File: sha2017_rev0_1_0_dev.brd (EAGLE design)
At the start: 95 x 86 mm, 200 parts, among them IC1 CP210X_USB_UART, IC2 AP7215, IC3 ESP32WROOM32, IC4 MCP73833, IC5 FXL6408, IC6 CPT112, Q2 MMBT2222A, Q3 MMBT2222A, Q4 MMBT2222A, Q5 MMBT2222A, Q6 SI1304 BDL, Q7 MMBT2222A, T1 SI2301DS, T2 SI2301DS, T3 SI2301DS, X1 2908-05WB-MG, X3 JST-PH3

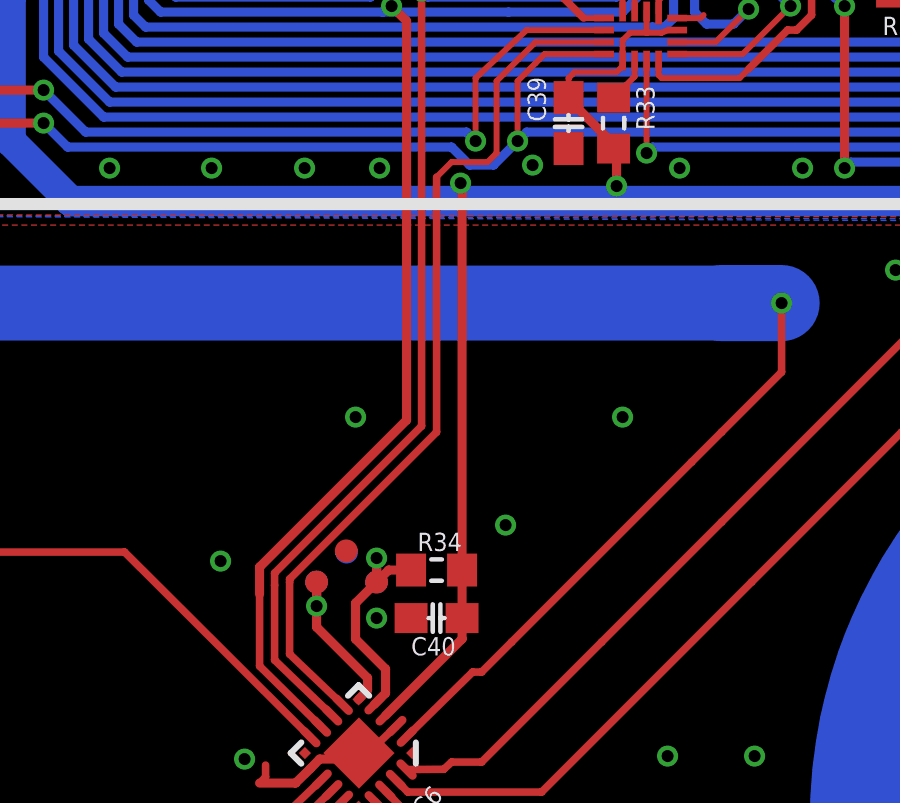
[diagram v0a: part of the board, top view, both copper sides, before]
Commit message: added 4,7µF decopling capacitor to the cpt112s power rails
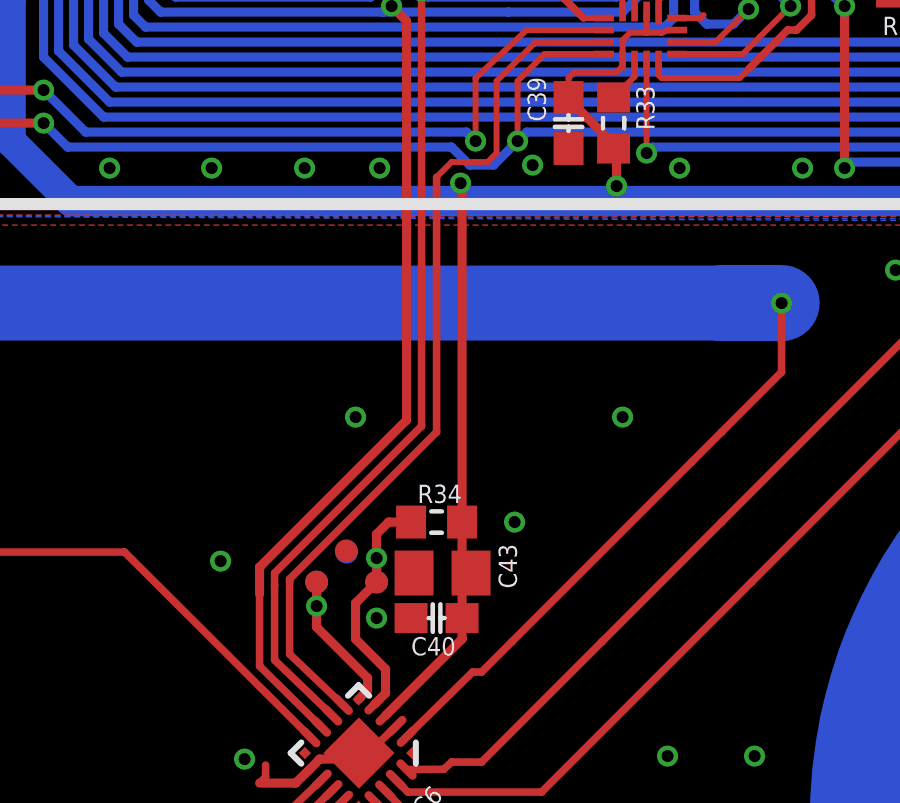
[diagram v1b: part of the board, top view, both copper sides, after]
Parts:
- added C43: 4u7/16V, rcl:C0805
- moved R34 1.60 mm to (43.5, 30.0)
- moved $$U$1 0.32 mm to (46.1, 30.0)
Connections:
- net +3V3: now also C43.1
- net GND: now also C43.2
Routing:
- net N$61: track 7.84 -> 8.64 mm
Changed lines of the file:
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@@
 <attribute name="PARTNO" value="NAP" x="39.5" y="28" size="1.778" layer="27" display="off"/>
 </element>
-<element name="R34" library="sha2017_rev0_1_0_dev" package="R0603-DASHES" value="1k" x="43.5" y="28.4" smashed="yes">
-<attribute name="NAME" x="42.865" y="29.035" size="0.6096" layer="25" font="vector" ratio="16"/>
-<attribute name="VALUE" x="42.865" y="26.495" size="1.27" layer="27"/>
-<attribute name="PARTNO" value="ERJ-3GEYJ102V" x="43.5" y="28.4" size="1.778" layer="27" display="off"/>
+<element name="R34" library="sha2017_rev0_1_0_dev" package="R0603-DASHES" value="1k" x="43.5" y="30" smashed="yes">
+<attribute name="NAME" x="42.865" y="30.635" size="0.6096" layer="25" font="vector" ratio="16"/>
+<attribute name="VALUE" x="42.865" y="28.095" size="1.27" layer="27"/>
+<attribute name="PARTNO" value="ERJ-3GEYJ102V" x="43.5" y="30" size="1.778" layer="27" display="off"/>
 </element>
 <element name="Q7" library="SparkFun-DiscreteSemi" package="SOT23-3" value="MMBT2222A" x="21" y="52.1" smashed="yes" rot="R180">
@@
 <attribute name="PARTNO" value="NAP" x="37.1" y="22.1" size="1.778" layer="27" display="off"/>
 </element>
-<element name="$$U$1" library="badge" package="VIA" value="VIA" x="45.8" y="29.9" smashed="yes">
-<attribute name="PARTNO" value="NAP" x="45.8" y="29.9" size="1.778" layer="27" display="off"/>
+<element name="$$U$1" library="badge" package="VIA" value="VIA" x="46.1" y="30" smashed="yes">
+<attribute name="PARTNO" value="NAP" x="46.1" y="30" size="1.778" layer="27" display="off"/>
 </element>
 <element name="U$4" library="badge" package="VIA" value="VIA" x="28.4" y="33.5" smashed="yes">
@@
 <attribute name="NAME" x="16.892" y="54.67" size="0.8128" layer="25" font="vector" ratio="16"/>
 <attribute name="VALUE" x="16.249" y="57.708" size="0.4064" layer="27" rot="R270"/>
+</element>
+<element name="C43" library="rcl" package="C0805" value="4u7/16V" x="43.7" y="28.3" smashed="yes" rot="R180">
+<attribute name="PARTNO" value="GRM21BR61C475KA88K" x="43.7" y="28.3" size="1.778" layer="27" rot="R180" display="off"/>
+<attribute name="NAME" x="45.57" y="29.27" size="0.6096" layer="25" font="vector" ratio="15" rot="R270"/>
+<attribute name="VALUE" x="44.97" y="30.84" size="1.27" layer="27" rot="R180"/>
 </element>
 </elements>
@@
 <contactref element="TP3" pad="P$1"/>
 <via x="64.9" y="71.32" extent="1-16" drill="0.4"/>
+<contactref element="C43" pad="2"/>
 <wire x1="40.49" y1="29.04" x2="40.5" y2="29" width="0" layer="19" extent="1-16"/>
 </signal>
@@
 <wire x1="49.5" y1="41.2" x2="49.3" y2="41" width="0.3048" layer="16"/>
 <wire x1="49.3" y1="41" x2="49.3" y2="40.7" width="0.3048" layer="16"/>
-<wire x1="44.35" y1="28.4" x2="44.35" y2="26.8" width="0.3048" layer="1"/>
+<wire x1="44.35" y1="30" x2="44.35" y2="28.2" width="0.3048" layer="1"/>
+<wire x1="44.35" y1="28.2" x2="44.35" y2="26.8" width="0.3048" layer="1"/>
 <wire x1="44.35" y1="26.8" x2="44.35" y2="26.10355625" width="0.3048" layer="1"/>
 <wire x1="44.35" y1="26.10355625" x2="41.80455" y2="23.55810625" width="0.3048" layer="1"/>
-<wire x1="44.35" y1="28.4" x2="44.35" y2="41.25" width="0.3048" layer="1"/>
+<wire x1="44.35" y1="30" x2="44.35" y2="41.25" width="0.3048" layer="1"/>
 <wire x1="44.35" y1="41.25" x2="44.3" y2="41.3" width="0.3048" layer="1"/>
 <via x="44.3" y="41.3" extent="1-16" drill="0.4"/>
@@
 <wire x1="20.9" y1="48.6" x2="23.25" y2="48.6" width="0.6096" layer="1"/>
 <wire x1="23.25" y1="48.6" x2="23.8" y2="48.05" width="0.6096" layer="1"/>
+<contactref element="C43" pad="1"/>
+<wire x1="44.65" y1="28.3" x2="44.408578125" y2="28.2" width="0.3048" layer="1" curve="-45"/>
+<wire x1="44.408578125" y1="28.2" x2="44.35" y2="28.2" width="0.3048" layer="1"/>
 </signal>
 <signal name="GDR">
@@
 <wire x1="41.8" y1="24.3" x2="41.8" y2="25.1" width="0.3048" layer="1"/>
 <wire x1="41.8" y1="25.1" x2="40.8" y2="26.1" width="0.3048" layer="1"/>
-<wire x1="41.5" y1="28" x2="41.9" y2="28.4" width="0.3048" layer="1"/>
-<wire x1="41.9" y1="28.4" x2="42.65" y2="28.4" width="0.3048" layer="1"/>
 <contactref element="TP100" pad="P$1"/>
 <wire x1="40.8" y1="26.1" x2="40.8" y2="27.3" width="0.3048" layer="1"/>
@@
 <via x="41.5" y="28.8" extent="1-16" drill="0.4"/>
 <wire x1="41.5" y1="28.8" x2="41.5" y2="28" width="0.3048" layer="16"/>
+<wire x1="42.65" y1="30" x2="41.9" y2="30" width="0.3048" layer="1"/>
+<wire x1="41.9" y1="30" x2="41.5" y2="29.6" width="0.3048" layer="1"/>
+<wire x1="41.5" y1="29.6" x2="41.5" y2="28.8" width="0.3048" layer="1"/>
 </signal>
 <signal name="N$62">

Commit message: minor adjustments
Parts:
- moved C43 0.10 mm to (43.7, 28.4)
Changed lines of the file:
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@@
 <attribute name="VALUE" x="16.249" y="57.708" size="0.4064" layer="27" rot="R270"/>
 </element>
-<element name="C43" library="rcl" package="C0805" value="4u7/16V" x="43.7" y="28.3" smashed="yes" rot="R180">
-<attribute name="PARTNO" value="GRM21BR61C475KA88K" x="43.7" y="28.3" size="1.778" layer="27" rot="R180" display="off"/>
-<attribute name="NAME" x="45.57" y="29.27" size="0.6096" layer="25" font="vector" ratio="15" rot="R270"/>
-<attribute name="VALUE" x="44.97" y="30.84" size="1.27" layer="27" rot="R180"/>
+<element name="C43" library="rcl" package="C0805" value="4u7/16V" x="43.7" y="28.4" smashed="yes" rot="R180">
+<attribute name="PARTNO" value="GRM21BR61C475KA88K" x="43.7" y="28.4" size="1.778" layer="27" rot="R180" display="off"/>
+<attribute name="NAME" x="45.57" y="29.37" size="0.6096" layer="25" font="vector" ratio="15" rot="R270"/>
+<attribute name="VALUE" x="44.97" y="30.94" size="1.27" layer="27" rot="R180"/>
 </element>
 </elements>
@@
 <wire x1="23.25" y1="48.6" x2="23.8" y2="48.05" width="0.6096" layer="1"/>
 <contactref element="C43" pad="1"/>
-<wire x1="44.65" y1="28.3" x2="44.408578125" y2="28.2" width="0.3048" layer="1" curve="-45"/>
+<wire x1="44.65" y1="28.4" x2="44.408578125" y2="28.2" width="0.3048" layer="1" curve="-45"/>
 <wire x1="44.408578125" y1="28.2" x2="44.35" y2="28.2" width="0.3048" layer="1"/>
 </signal>

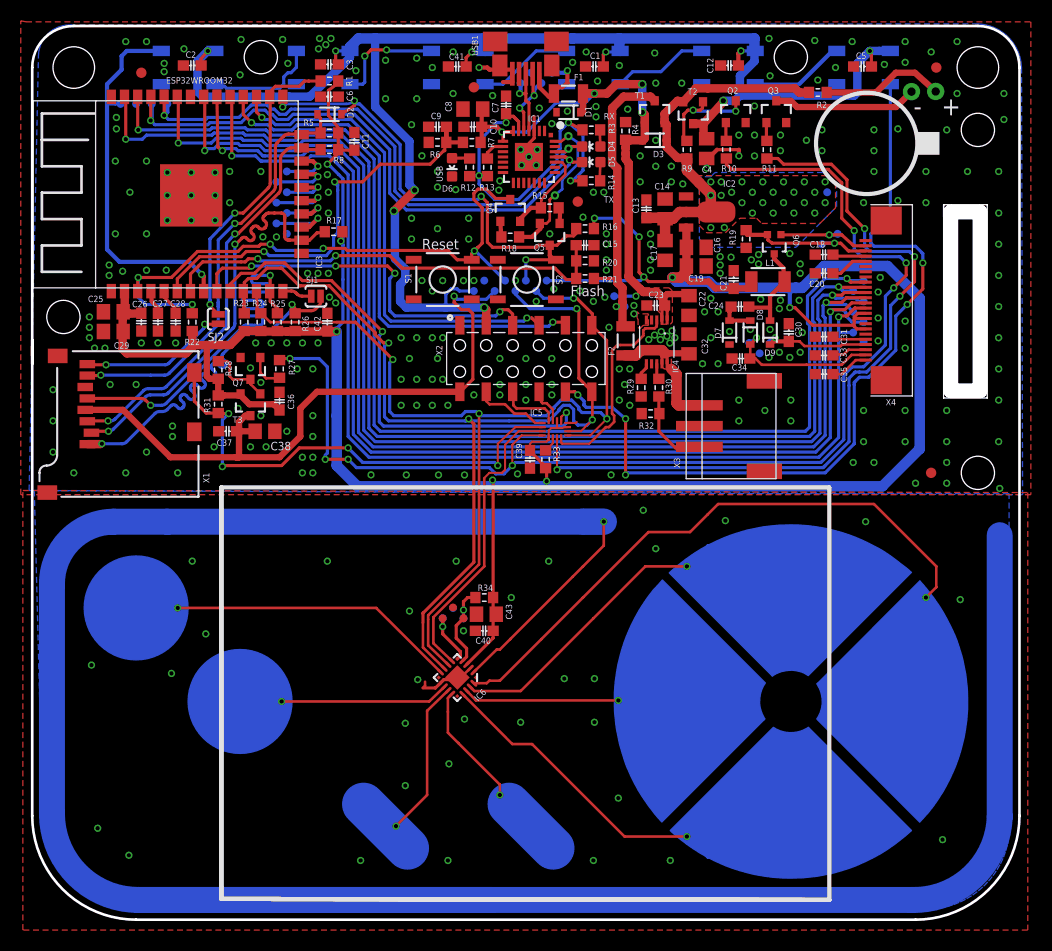
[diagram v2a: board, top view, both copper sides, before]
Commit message: SD pullups to 3V3_SWITCHED
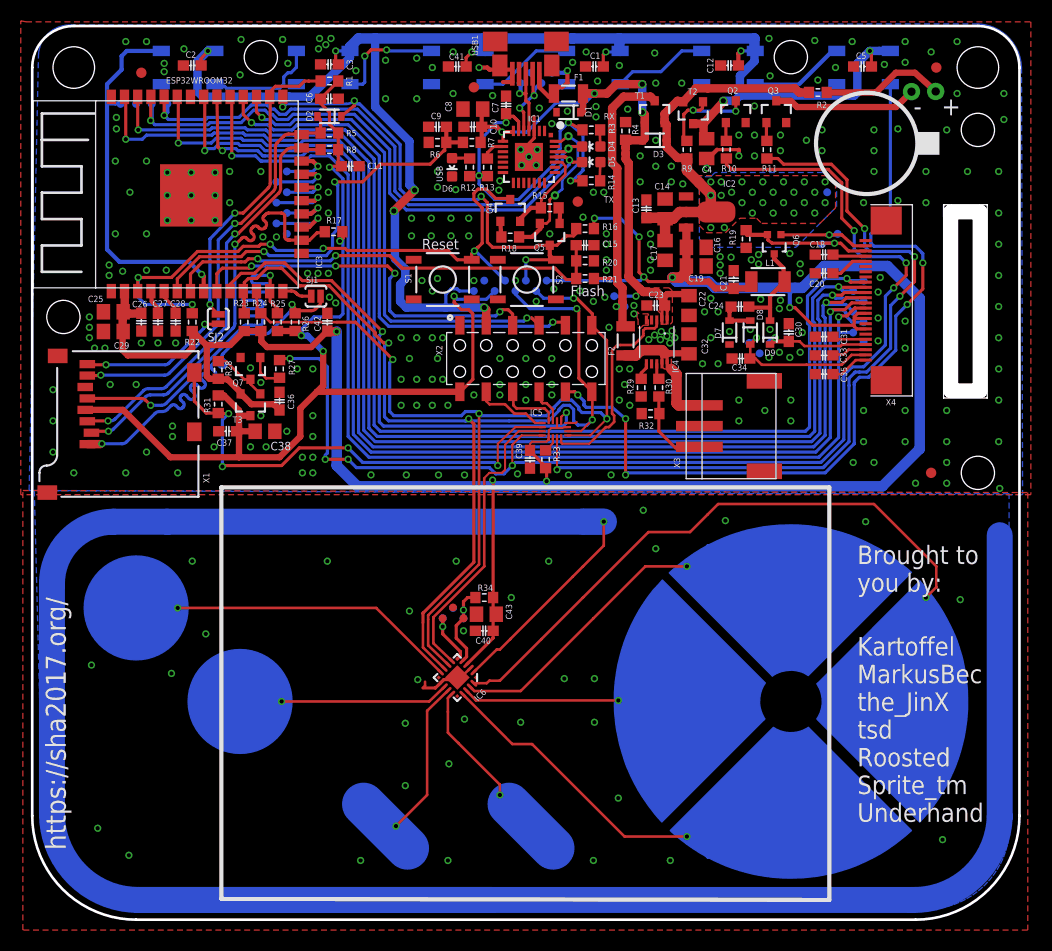
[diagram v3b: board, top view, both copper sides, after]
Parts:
- moved C11 2.43 mm to (30.6, 71.5), turned to 0 degrees
- moved C6 0.20 mm to (28.6, 78.0)
- moved D2 0.20 mm to (28.6, 76.3)
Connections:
- net +3V3: no longer C11.1, C6.1, R1.2, R17.2, R25.2, R26.2, R31.1, R5.2, R8.2
- net 3V3_SWITCHED: now also C11.1, C6.1, R1.2, R17.2, R25.2, R26.2, R31.1, R5.2, R8.2
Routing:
- net 3V3_SWITCHED: track 65.1 -> 110.0 mm, vias 1 -> 5
- net +3V3: track 270.8 -> 239.1 mm, vias 10 -> 8
- net VUSB_SENSE: track 42.1 -> 40.6 mm
- net N$17: track 6.32 -> 5.62 mm
- net SD_DATA0: track 41.5 -> 40.9 mm
- net GND: vias 304 -> 297
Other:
- outline, holes or cut-outs redrawn
- board text added: "Brought to you by:"
- board text added: "Kartoffel MarkusBec the_JinX tsd Roosted Sprite_tm Underhand"
- board text added: "https://sha2017.org/"

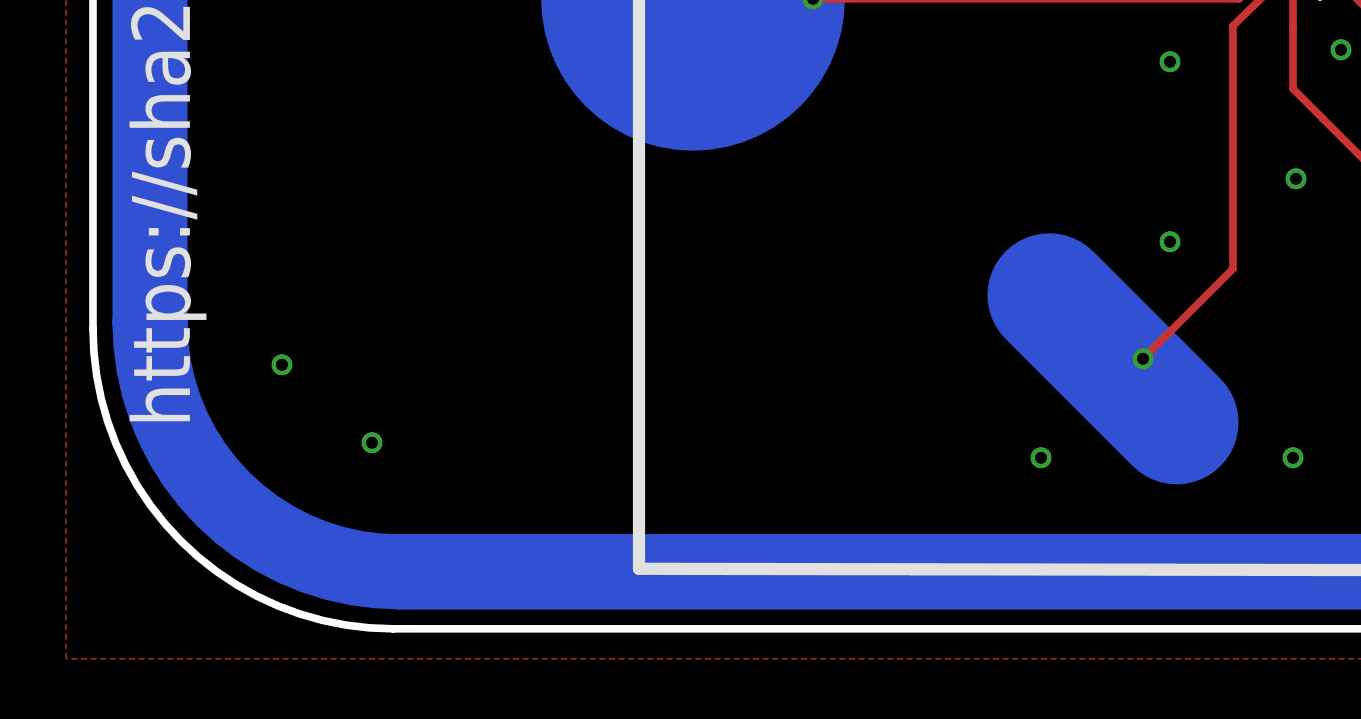
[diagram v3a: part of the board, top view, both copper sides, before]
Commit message: Added some artwork
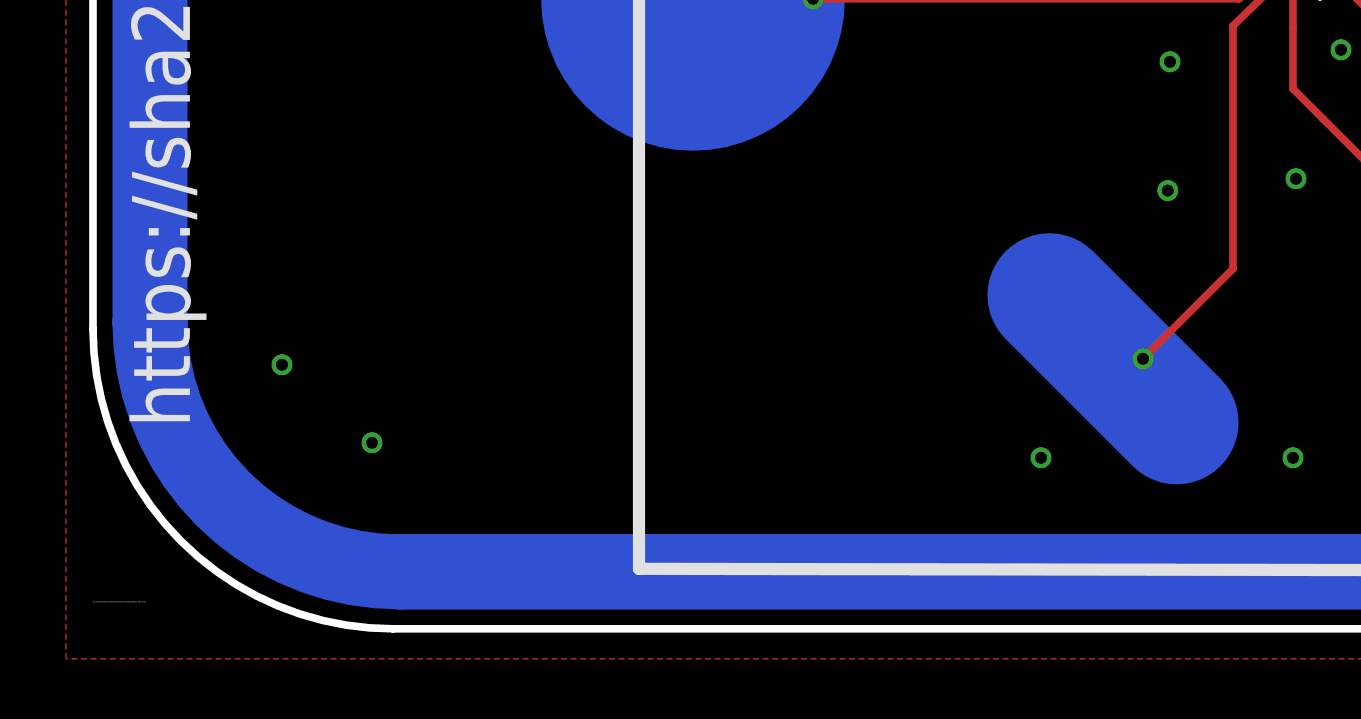
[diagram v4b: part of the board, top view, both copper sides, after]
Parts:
- moved U$17 1.71 mm to (35.8, 13.6)
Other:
- board text added: "/home/niek/Sync/Projects/SHA2017-badge/diyart-1bit.bmp"
- board text added: "A"
- board text added: "B"
- board text added: "Select"
- board text added: "Start"
